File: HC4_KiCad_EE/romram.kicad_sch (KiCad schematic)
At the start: 6 parts, among them IC1 ATmega4809-A, IC2 CH340E, J2 AVR-UPDI-6

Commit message: 完成かも～
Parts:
- added CP14, CP15, CP16: 0.1u, symbol Device2:C_Bypass
- renumbered C5 to C2, IC1 to IC14, IC2 to IC15, J2 to J5, LD22 to LD31, R13 to R3
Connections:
- net GND: now also CP14.2, CP15.2, CP16.2
- net VCC: now also CP14.1, CP15.1, CP16.1
- net ~{PORTA_IN_OE} renamed ~{PORT_IN_OE}

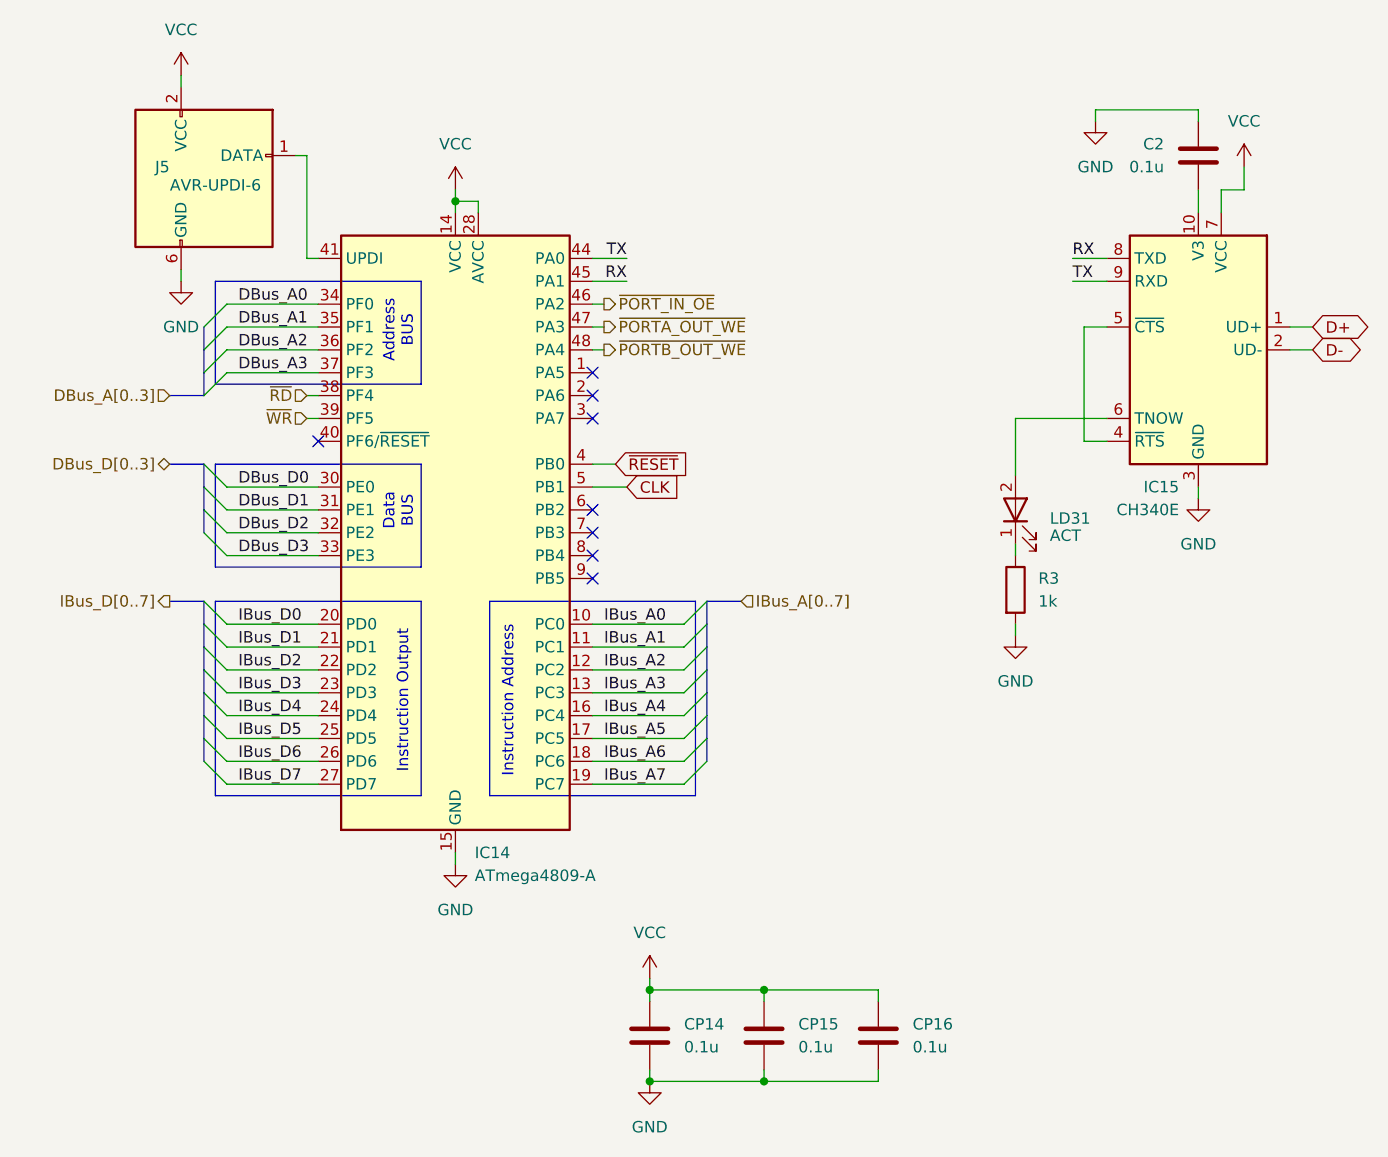
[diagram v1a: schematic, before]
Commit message: Carry_ENを論理反転、回路図の修正
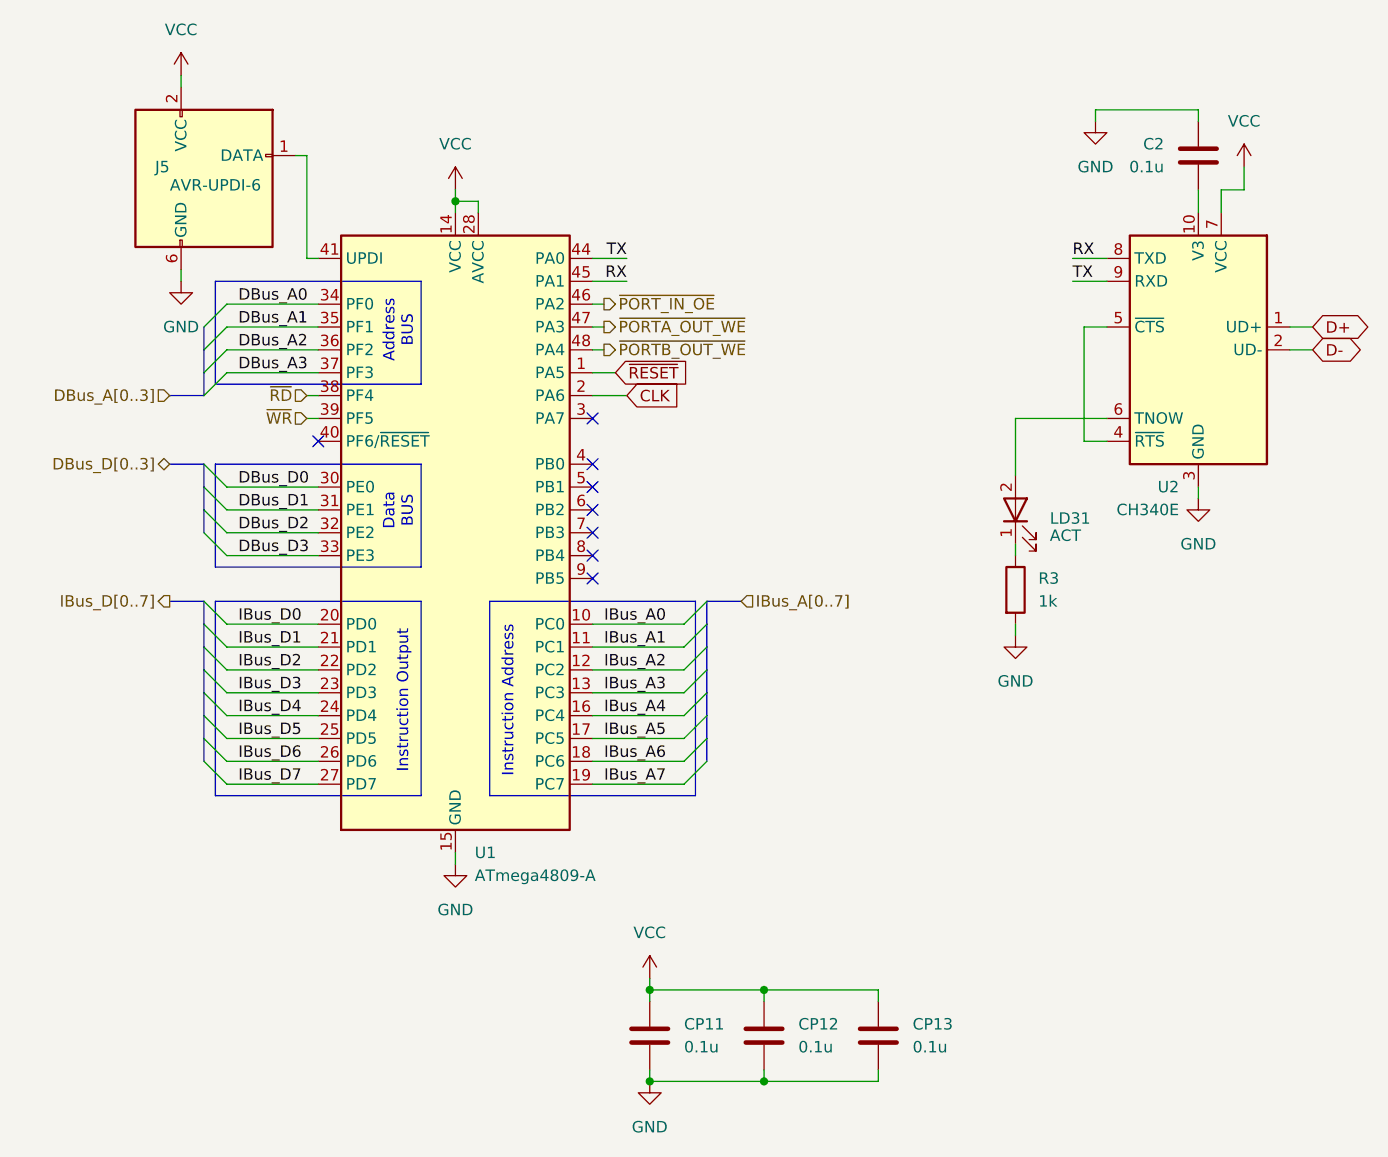
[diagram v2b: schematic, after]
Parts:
- renumbered CP14 to CP11, CP15 to CP12, CP16 to CP13, IC14 to U1, IC15 to U2
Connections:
- net CLK: now also U1.2 (PA6); no longer U1.5 (PB1)
- net ~{RESET}: now also U1.1 (PA5); no longer U1.4 (PB0)
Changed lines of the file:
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@@
+	)
+	(no_connect
+		(at 100.33 102.87)
 	)
 	(no_connect
@@
 	)
 	(no_connect
-		(at 100.33 90.17)
-	)
-	(no_connect
-		(at 100.33 92.71)
+		(at 100.33 100.33)
 	)
 	(bus_entry
@@
 	(wire
 		(pts
-			(xy 100.33 102.87) (xy 104.14 102.87)
-		)
-		(stroke
-			(width 0)
-			(type default)
-		)
-	)
-	(wire
-		(pts
 			(xy 85.09 143.51) (xy 85.09 144.78)
 		)
@@
 	(wire
 		(pts
-			(xy 100.33 100.33) (xy 102.87 100.33)
-		)
-		(stroke
-			(width 0)
-			(type default)
-		)
-	)
-	(wire
-		(pts
 			(xy 67.31 66.04) (xy 68.58 66.04)
 		)
@@
 	(wire
 		(pts
+			(xy 100.33 90.17) (xy 102.87 90.17)
+		)
+		(stroke
+			(width 0)
+			(type default)
+		)
+	)
+	(wire
+		(pts
 			(xy 68.58 95.25) (xy 69.85 95.25)
 		)
@@
 		(pts
 			(xy 59.69 107.95) (xy 69.85 107.95)
+		)
+		(stroke
+			(width 0)
+			(type default)
+		)
+	)
+	(wire
+		(pts
+			(xy 100.33 92.71) (xy 104.14 92.71)
 		)
 		(stroke
@@
 	(global_label "CLK"
 		(shape input)
-		(at 104.14 102.87 0)
+		(at 104.14 92.71 0)
 		(fields_autoplaced yes)
 		(effects
@@
 		)
 		(property "Intersheetrefs" "${INTERSHEET_REFS}"
-			(at 110.6933 102.87 0)
+			(at 110.6933 92.71 0)
+			(effects
+				(font
+					(size 1.27 1.27)
+				)
+				(justify left)
+				(hide yes)
+			)
+		)
+	)
+	(global_label "~{RESET}"
+		(shape input)
+		(at 102.87 90.17 0)
+		(fields_autoplaced yes)
+		(effects
+			(font
+				(size 1.27 1.27)
+			)
+			(justify left)
+		)
+		(property "Intersheetrefs" "${INTERSHEET_REFS}"
+			(at 111.6003 90.17 0)
 			(effects
 				(font
@@
 		(property "Intersheetrefs" "${INTERSHEET_REFS}"
 			(at 187.2789 87.63 0)
-			(effects
-				(font
-					(size 1.27 1.27)
-				)
-				(justify left)
-				(hide yes)
-			)
-		)
-	)
-	(global_label "~{RESET}"
-		(shape input)
-		(at 102.87 100.33 0)
-		(fields_autoplaced yes)
-		(effects
-			(font
-				(size 1.27 1.27)
-			)
-			(justify left)
-		)
-		(property "Intersheetrefs" "${INTERSHEET_REFS}"
-			(at 111.6003 100.33 0)
 			(effects
 				(font
@@
 		(dnp no)
 		(fields_autoplaced yes)
-		(property "Reference" "#PWR052"
+		(property "Reference" "#PWR048"
 			(at 147.32 125.73 0)
 			(effects
@@
 			(project ""
 				(path "/33731ded-38c0-4297-bdd8-92b082f46ff8/ee79785c-5138-4152-a60d-370cd803a828"
-					(reference "#PWR052")
+					(reference "#PWR048")
 					(unit 1)
 				)
@@
 		(dnp no)
 		(fields_autoplaced yes)
-		(property "Reference" "#PWR049"
+		(property "Reference" "#PWR043"
 			(at 54.61 86.36 0)
 			(effects
@@
 			(project ""
 				(path "/33731ded-38c0-4297-bdd8-92b082f46ff8/ee79785c-5138-4152-a60d-370cd803a828"
-					(reference "#PWR049")
+					(reference "#PWR043")
 					(unit 1)
 				)
@@
 		(dnp no)
 		(fields_autoplaced yes)
-		(property "Reference" "CP14"
+		(property "Reference" "CP11"
 			(at 110.49 162.5599 0)
 			(effects
@@
 			(project ""
 				(path "/33731ded-38c0-4297-bdd8-92b082f46ff8/ee79785c-5138-4152-a60d-370cd803a828"
-					(reference "CP14")
+					(reference "CP11")
 					(unit 1)
 				)
@@
 		(dnp no)
 		(fields_autoplaced yes)
-		(property "Reference" "#PWR048"
+		(property "Reference" "#PWR042"
 			(at 54.61 60.96 0)
 			(effects
@@
 			(project ""
 				(path "/33731ded-38c0-4297-bdd8-92b082f46ff8/ee79785c-5138-4152-a60d-370cd803a828"
-					(reference "#PWR048")
+					(reference "#PWR042")
 					(unit 1)
 				)
@@
 		(dnp no)
 		(fields_autoplaced yes)
-		(property "Reference" "CP15"
+		(property "Reference" "CP12"
 			(at 123.19 162.5599 0)
 			(effects
@@
 			(project "HC4_KiCad_EE"
 				(path "/33731ded-38c0-4297-bdd8-92b082f46ff8/ee79785c-5138-4152-a60d-370cd803a828"
-					(reference "CP15")
+					(reference "CP12")
 					(unit 1)
 				)
@@
 		(dnp no)
 		(fields_autoplaced yes)
-		(property "Reference" "#PWR050"
+		(property "Reference" "#PWR044"
 			(at 85.09 73.66 0)
 			(effects
@@
 			(project "HC4_KiCad_EE"
 				(path "/33731ded-38c0-4297-bdd8-92b082f46ff8/ee79785c-5138-4152-a60d-370cd803a828"
-					(reference "#PWR050")
+					(reference "#PWR044")
 					(unit 1)
 				)
@@
 		(dnp no)
 		(fields_autoplaced yes)
-		(property "Reference" "#PWR051"
+		(property "Reference" "#PWR045"
 			(at 85.09 151.13 0)
 			(effects
@@
 			(project "HC4_KiCad_EE"
 				(path "/33731ded-38c0-4297-bdd8-92b082f46ff8/ee79785c-5138-4152-a60d-370cd803a828"
-					(reference "#PWR051")
+					(reference "#PWR045")
 					(unit 1)
 				)
@@
 		(dnp no)
 		(fields_autoplaced yes)
-		(property "Reference" "#PWR066"
+		(property "Reference" "#PWR046"
 			(at 106.68 161.29 0)
 			(effects
@@
 			(project ""
 				(path "/33731ded-38c0-4297-bdd8-92b082f46ff8/ee79785c-5138-4152-a60d-370cd803a828"
-					(reference "#PWR066")
+					(reference "#PWR046")
 					(unit 1)
 				)
@@
 		(on_board yes)
 		(dnp no)
-		(property "Reference" "IC15"
+		(property "Reference" "U2"
 			(at 165.4967 102.87 0)
 			(effects
@@
 			(project "HC4_KiCad_EE"
 				(path "/33731ded-38c0-4297-bdd8-92b082f46ff8/ee79785c-5138-4152-a60d-370cd803a828"
-					(reference "IC15")
+					(reference "U2")
 					(unit 1)
 				)
@@
 		(dnp no)
 		(fields_autoplaced yes)
-		(property "Reference" "#PWR055"
+		(property "Reference" "#PWR051"
 			(at 172.72 71.12 0)
 			(effects
@@
 			(project ""
 				(path "/33731ded-38c0-4297-bdd8-92b082f46ff8/ee79785c-5138-4152-a60d-370cd803a828"
-					(reference "#PWR055")
+					(reference "#PWR051")
 					(unit 1)
 				)
@@
 		(dnp no)
 		(fields_autoplaced yes)
-		(property "Reference" "#PWR054"
+		(property "Reference" "#PWR050"
 			(at 167.64 110.49 0)
 			(effects
@@
 			(project ""
 				(path "/33731ded-38c0-4297-bdd8-92b082f46ff8/ee79785c-5138-4152-a60d-370cd803a828"
-					(reference "#PWR054")
+					(reference "#PWR050")
 					(unit 1)
 				)
@@
 		(dnp no)
 		(fields_autoplaced yes)
-		(property "Reference" "#PWR053"
+		(property "Reference" "#PWR049"
 			(at 156.21 68.58 0)
 			(effects
@@
 			(project ""
 				(path "/33731ded-38c0-4297-bdd8-92b082f46ff8/ee79785c-5138-4152-a60d-370cd803a828"
-					(reference "#PWR053")
+					(reference "#PWR049")
 					(unit 1)
 				)
@@
 		(dnp no)
 		(fields_autoplaced yes)
-		(property "Reference" "IC14"
+		(property "Reference" "U1"
 			(at 87.2333 143.51 0)
 			(effects
@@
 			(project "HC4_KiCad_EE"
 				(path "/33731ded-38c0-4297-bdd8-92b082f46ff8/ee79785c-5138-4152-a60d-370cd803a828"
-					(reference "IC14")
+					(reference "U1")
 					(unit 1)
 				)
@@
 		(dnp no)
 		(fields_autoplaced yes)
-		(property "Reference" "CP16"
+		(property "Reference" "CP13"
 			(at 135.89 162.5599 0)
 			(effects
@@
 			(project "HC4_KiCad_EE"
 				(path "/33731ded-38c0-4297-bdd8-92b082f46ff8/ee79785c-5138-4152-a60d-370cd803a828"
-					(reference "CP16")
+					(reference "CP13")
 					(unit 1)
 				)
@@
 		(dnp no)
 		(fields_autoplaced yes)
-		(property "Reference" "#PWR067"
+		(property "Reference" "#PWR047"
 			(at 106.68 175.26 0)
 			(effects
@@
 			(project ""
 				(path "/33731ded-38c0-4297-bdd8-92b082f46ff8/ee79785c-5138-4152-a60d-370cd803a828"
-					(reference "#PWR067")
+					(reference "#PWR047")
 					(unit 1)
 				)

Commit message: PortBを4511に、フットプリントの割り付け開始
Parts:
- C2, CP11, CP12, CP13: footprint (none) -> Capacitor_SMD:C_0603_1608Metric
- renumbered J5 to J4, R3 to R10
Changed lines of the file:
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@@
 		(dnp no)
 		(fields_autoplaced yes)
-		(property "Reference" "#PWR048"
+		(property "Reference" "#PWR050"
 			(at 147.32 125.73 0)
 			(effects
@@
 			(project ""
 				(path "/33731ded-38c0-4297-bdd8-92b082f46ff8/ee79785c-5138-4152-a60d-370cd803a828"
-					(reference "#PWR048")
+					(reference "#PWR050")
 					(unit 1)
 				)
@@
 		(on_board yes)
 		(dnp no)
-		(property "Reference" "J5"
+		(property "Reference" "J4"
 			(at 53.34 67.31 0)
 			(effects
@@
 			(project "HC4_KiCad_EE"
 				(path "/33731ded-38c0-4297-bdd8-92b082f46ff8/ee79785c-5138-4152-a60d-370cd803a828"
-					(reference "J5")
+					(reference "J4")
 					(unit 1)
 				)
@@
 		(dnp no)
 		(fields_autoplaced yes)
-		(property "Reference" "#PWR043"
+		(property "Reference" "#PWR045"
 			(at 54.61 86.36 0)
 			(effects
@@
 			(project ""
 				(path "/33731ded-38c0-4297-bdd8-92b082f46ff8/ee79785c-5138-4152-a60d-370cd803a828"
-					(reference "#PWR043")
+					(reference "#PWR045")
 					(unit 1)
 				)
@@
 			)
 		)
-		(property "Footprint" ""
+		(property "Footprint" "Capacitor_SMD:C_0603_1608Metric"
 			(at 166.6748 69.85 0)
 			(effects
@@
 		(dnp no)
 		(fields_autoplaced yes)
-		(property "Reference" "R3"
+		(property "Reference" "R10"
 			(at 149.86 113.0299 0)
 			(effects
@@
 			(project ""
 				(path "/33731ded-38c0-4297-bdd8-92b082f46ff8/ee79785c-5138-4152-a60d-370cd803a828"
-					(reference "R3")
+					(reference "R10")
 					(unit 1)
 				)
@@
 			)
 		)
-		(property "Footprint" ""
+		(property "Footprint" "Capacitor_SMD:C_0603_1608Metric"
 			(at 107.6452 167.64 0)
 			(effects
@@
 		(dnp no)
 		(fields_autoplaced yes)
-		(property "Reference" "#PWR042"
+		(property "Reference" "#PWR044"
 			(at 54.61 60.96 0)
 			(effects
@@
 			(project ""
 				(path "/33731ded-38c0-4297-bdd8-92b082f46ff8/ee79785c-5138-4152-a60d-370cd803a828"
-					(reference "#PWR042")
+					(reference "#PWR044")
 					(unit 1)
 				)
@@
 			)
 		)
-		(property "Footprint" ""
+		(property "Footprint" "Capacitor_SMD:C_0603_1608Metric"
 			(at 120.3452 167.64 0)
 			(effects
@@
 		(dnp no)
 		(fields_autoplaced yes)
-		(property "Reference" "#PWR044"
+		(property "Reference" "#PWR046"
 			(at 85.09 73.66 0)
 			(effects
@@
 			(project "HC4_KiCad_EE"
 				(path "/33731ded-38c0-4297-bdd8-92b082f46ff8/ee79785c-5138-4152-a60d-370cd803a828"
-					(reference "#PWR044")
+					(reference "#PWR046")
 					(unit 1)
 				)
@@
 		(dnp no)
 		(fields_autoplaced yes)
-		(property "Reference" "#PWR045"
+		(property "Reference" "#PWR047"
 			(at 85.09 151.13 0)
 			(effects
@@
 			(project "HC4_KiCad_EE"
 				(path "/33731ded-38c0-4297-bdd8-92b082f46ff8/ee79785c-5138-4152-a60d-370cd803a828"
-					(reference "#PWR045")
+					(reference "#PWR047")
 					(unit 1)
 				)
@@
 		(dnp no)
 		(fields_autoplaced yes)
-		(property "Reference" "#PWR046"
+		(property "Reference" "#PWR048"
 			(at 106.68 161.29 0)
 			(effects
@@
 			(project ""
 				(path "/33731ded-38c0-4297-bdd8-92b082f46ff8/ee79785c-5138-4152-a60d-370cd803a828"
-					(reference "#PWR046")
+					(reference "#PWR048")
 					(unit 1)
 				)
@@
 		(dnp no)
 		(fields_autoplaced yes)
-		(property "Reference" "#PWR051"
+		(property "Reference" "#PWR053"
 			(at 172.72 71.12 0)
 			(effects
@@
 			(project ""
 				(path "/33731ded-38c0-4297-bdd8-92b082f46ff8/ee79785c-5138-4152-a60d-370cd803a828"
-					(reference "#PWR051")
+					(reference "#PWR053")
 					(unit 1)
 				)
@@
 		(dnp no)
 		(fields_autoplaced yes)
-		(property "Reference" "#PWR050"
+		(property "Reference" "#PWR052"
 			(at 167.64 110.49 0)
 			(effects
@@
 			(project ""
 				(path "/33731ded-38c0-4297-bdd8-92b082f46ff8/ee79785c-5138-4152-a60d-370cd803a828"
-					(reference "#PWR050")
+					(reference "#PWR052")
 					(unit 1)
 				)
@@
 		(dnp no)
 		(fields_autoplaced yes)
-		(property "Reference" "#PWR049"
+		(property "Reference" "#PWR051"
 			(at 156.21 68.58 0)
 			(effects
@@
 			(project ""
 				(path "/33731ded-38c0-4297-bdd8-92b082f46ff8/ee79785c-5138-4152-a60d-370cd803a828"
-					(reference "#PWR049")
+					(reference "#PWR051")
 					(unit 1)
 				)
@@
 			)
 		)
-		(property "Footprint" ""
+		(property "Footprint" "Capacitor_SMD:C_0603_1608Metric"
 			(at 133.0452 167.64 0)
 			(effects
@@
 		(dnp no)
 		(fields_autoplaced yes)
-		(property "Reference" "#PWR047"
+		(property "Reference" "#PWR049"
 			(at 106.68 175.26 0)
 			(effects
@@
 			(project ""
 				(path "/33731ded-38c0-4297-bdd8-92b082f46ff8/ee79785c-5138-4152-a60d-370cd803a828"
-					(reference "#PWR047")
-					(unit 1)
-				)
+					(reference "#PWR049")
+					(unit 1)
+				)

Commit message: チップ集合抵抗に変更、基板作成開始
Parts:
- J4: footprint (none) -> Connector_PinHeader_2.54mm:PinHeader_2x03_P2.54mm_Vertical
- LD31: footprint (none) -> LED_SMD:LED_0603_1608Metric
- R3: renamed from R10; footprint (none) -> Resistor_SMD:R_0603_1608Metric
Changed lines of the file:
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@@
 	(title_block
 		(title "HC4_CPU")
-		(date "2025-02-23")
-		(rev "1.2")
+		(date "2025-06-16")
+		(rev "1.0")
 	)
 	(rectangle
@@
 			)
 		)
-		(property "Footprint" ""
+		(property "Footprint" "Connector_PinHeader_2.54mm:PinHeader_2x03_P2.54mm_Vertical"
 			(at 50.8 69.85 90)
 			(effects
@@
 		(dnp no)
 		(fields_autoplaced yes)
-		(property "Reference" "R10"
+		(property "Reference" "R3"
 			(at 149.86 113.0299 0)
 			(effects
@@
 			)
 		)
-		(property "Footprint" ""
+		(property "Footprint" "Resistor_SMD:R_0603_1608Metric"
 			(at 145.542 114.3 90)
 			(effects
@@
 			(project ""
 				(path "/33731ded-38c0-4297-bdd8-92b082f46ff8/ee79785c-5138-4152-a60d-370cd803a828"
-					(reference "R10")
+					(reference "R3")
 					(unit 1)
 				)
@@
 			)
 		)
-		(property "Footprint" ""
+		(property "Footprint" "LED_SMD:LED_0603_1608Metric"
 			(at 147.32 105.41 0)
 			(effects
